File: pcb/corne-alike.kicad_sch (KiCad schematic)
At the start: 45 parts, among them SW1 SW_PUSH, SW10 SW_PUSH, SW11 SW_PUSH, SW12 SW_PUSH, SW13 SW_PUSH, SW14 SW_PUSH, SW15 SW_PUSH, SW16 SW_PUSH, SW17 SW_PUSH, SW18 SW_PUSH, SW19 SW_PUSH, SW2 SW_PUSH, SW20 SW_PUSH, SW21 SW_PUSH, SW3 SW_PUSH, SW4 SW_PUSH, SW5 SW_PUSH, SW6 SW_PUSH, SW7 SW_PUSH, SW8 SW_PUSH, SW9 SW_PUSH, U1 nice_nano

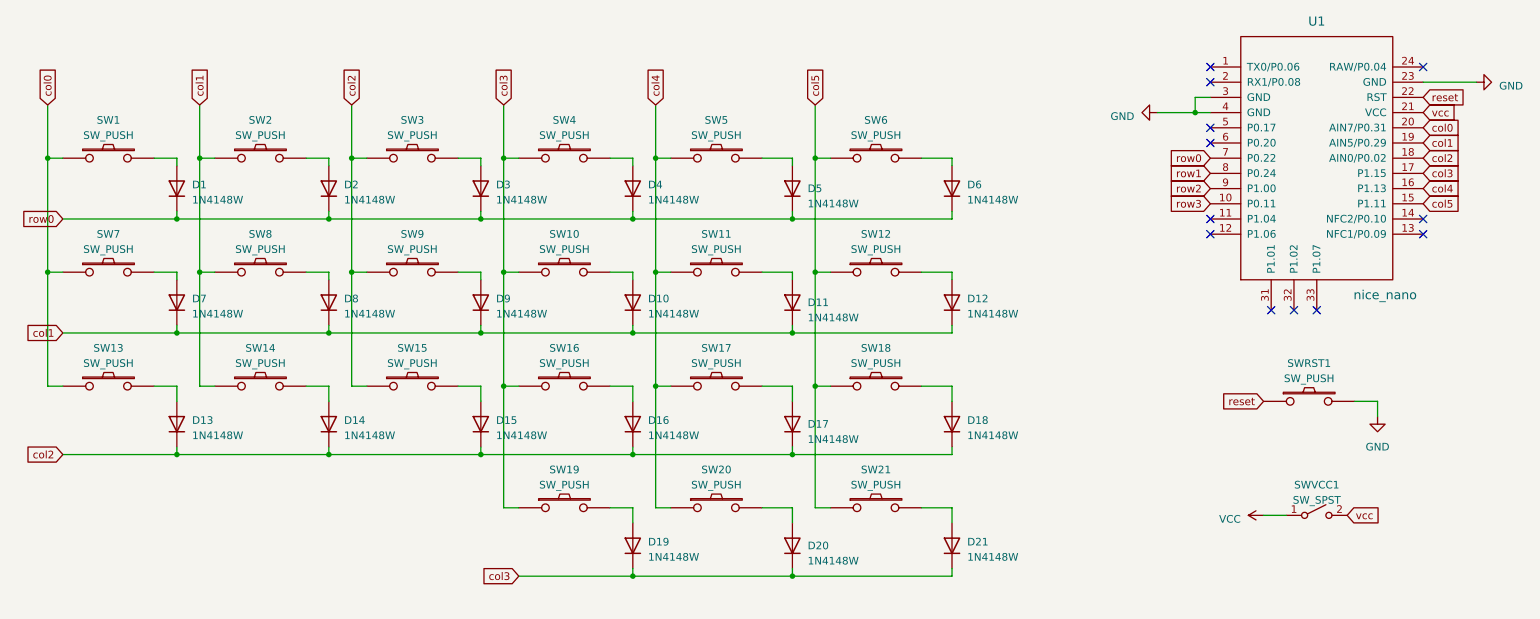
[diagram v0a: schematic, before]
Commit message: Associate footprints and generate pcb
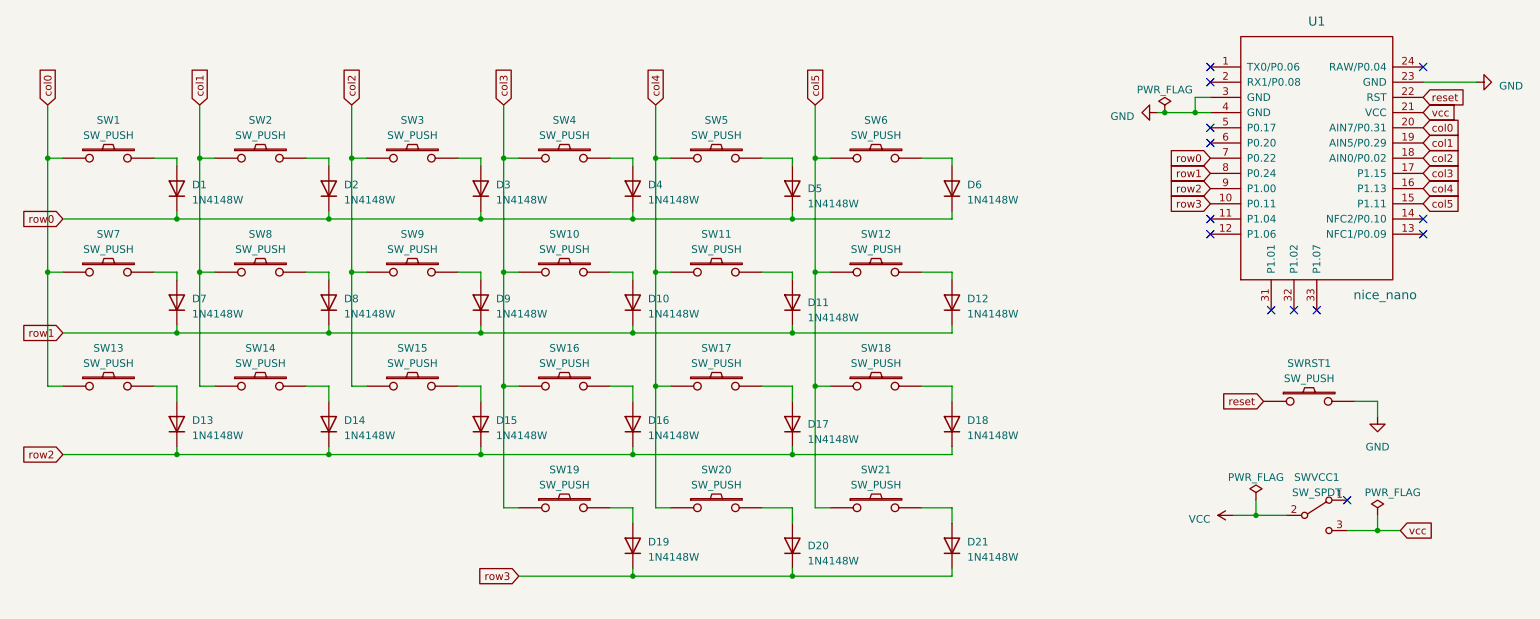
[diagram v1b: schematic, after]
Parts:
- removed SWVCC1: SW_SPST, symbol corne-alike:SW_SPST
- added SWVCC1: SW_SPDT, corne-alike:SW_EG1218, symbol corne-alike:SW_SPDT
- D1, D10, D11, D12, D13, D14, D15, D16, D17, D18, D19, D2, D20, D21, D3, D4, D5, D6, D7, D8, D9: footprint Diode_SMD:D_SOD-123 -> corne-alike:D_SOD-123
- SW1, SW10, SW11, SW12, SW13, SW14, SW15, SW16, SW17, SW18, SW19, SW2, SW20, SW21, SW3, SW4, SW5, SW6, SW7, SW8, SW9: footprint (none) -> corne-alike:Kailh_PG1350
- SWRST1: footprint (none) -> corne-alike:SW_TVBP06
- U1: footprint (none) -> corne-alike:nice_nano
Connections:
- net VCC: now also SWVCC1.2 (B)
- net col1: no longer D10.1 (K), D11.1 (K), D12.1 (K), D7.1 (K), D8.1 (K), D9.1 (K)
- net col2: no longer D13.1 (K), D14.1 (K), D15.1 (K), D16.1 (K), D17.1 (K), D18.1 (K)
- net col3: no longer D19.1 (K), D20.1 (K), D21.1 (K)
- net row1: now also D10.1 (K), D11.1 (K), D12.1 (K), D7.1 (K), D8.1 (K), D9.1 (K)
- net row2: now also D13.1 (K), D14.1 (K), D15.1 (K), D16.1 (K), D17.1 (K), D18.1 (K)
- net row3: now also D19.1 (K), D20.1 (K), D21.1 (K)
- net vcc: now also SWVCC1.3 (C)
- no-connect marks 12 -> 13

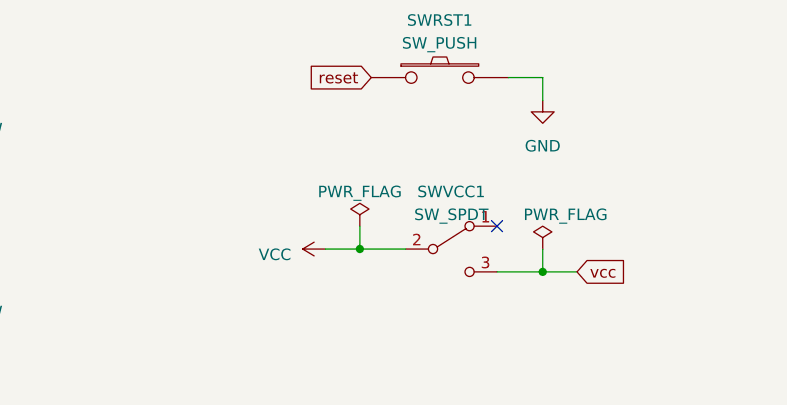
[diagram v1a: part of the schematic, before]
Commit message: Add bat connector, place reset, on/off and bat to pcb
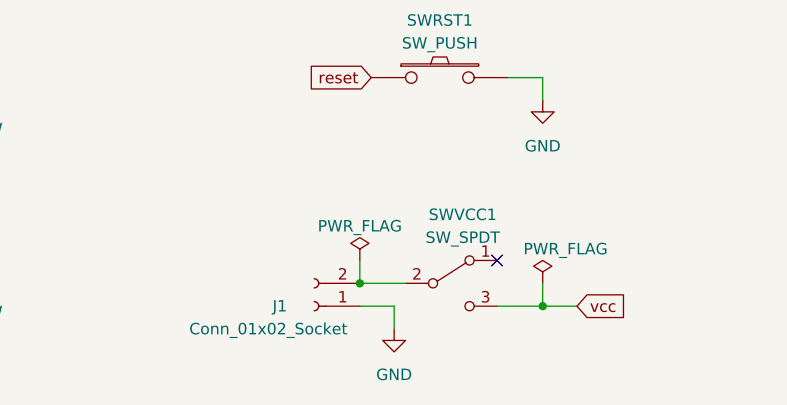
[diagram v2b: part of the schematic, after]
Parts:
- added J1: Conn_01x02_Socket, corne-alike:JST_PH_S2B-PH-SM4-TB_1x02-1MP_P2.00mm_Horizontal, symbol Connector:Conn_01x02_Socket
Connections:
- net GND: now also J1.1 (Pin_1)
- net VCC: no longer names the net of SWVCC1.2 (B)
- net VCC: now also J1.2 (Pin_2)
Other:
- moved on the sheet: SWVCC1
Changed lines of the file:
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@@
   (junction (at 120.65 107.95) (diameter 0) (color 0 0 0 0)
   )
+  (junction (at 224.79 101.6) (diameter 0) (color 0 0 0 0)
+  )
   (junction (at 95.25 48.26) (diameter 0) (color 0 0 0 0)
   )
@@
   (junction (at 99.06 57.15) (diameter 0) (color 0 0 0 0)
   )
-  (junction (at 224.79 97.79) (diameter 0) (color 0 0 0 0)
-  )
   (junction (at 95.25 67.31) (diameter 0) (color 0 0 0 0)
   )
@@
   (junction (at 151.13 38.1) (diameter 0) (color 0 0 0 0)
   )
-  (junction (at 245.11 100.33) (diameter 0) (color 0 0 0 0)
+  (junction (at 245.11 104.14) (diameter 0) (color 0 0 0 0)
   )
   (junction (at 22.86 38.1) (diameter 0) (color 0 0 0 0)
@@
   (no_connect (at 217.17 22.86))
   (no_connect (at 217.17 35.56))
-  (no_connect (at 240.03 95.25))
+  (no_connect (at 240.03 99.06))
   (no_connect (at 234.95 63.5))
   (no_connect (at 231.14 63.5))
@@
     (stroke (width 0) (type default))
   )
-  (wire (pts (xy 224.79 97.79) (xy 229.87 97.79))
+  (wire (pts (xy 224.79 101.6) (xy 229.87 101.6))
     (stroke (width 0) (type default))
   )
@@
     (stroke (width 0) (type default))
   )
+  (wire (pts (xy 228.6 106.68) (xy 228.6 104.14))
+    (stroke (width 0) (type default))
+  )
   (wire (pts (xy 25.4 87.63) (xy 44.45 87.63))
     (stroke (width 0) (type default))
@@
     (stroke (width 0) (type default))
   )
-  (wire (pts (xy 224.79 95.25) (xy 224.79 97.79))
+  (wire (pts (xy 224.79 99.06) (xy 224.79 101.6))
     (stroke (width 0) (type default))
   )
@@
     (stroke (width 0) (type default))
   )
+  (wire (pts (xy 228.6 104.14) (xy 224.79 104.14))
+    (stroke (width 0) (type default))
+  )
   (wire (pts (xy 142.24 96.52) (xy 147.32 96.52))
     (stroke (width 0) (type default))
@@
     (stroke (width 0) (type default))
   )
-  (wire (pts (xy 240.03 100.33) (xy 245.11 100.33))
+  (wire (pts (xy 240.03 104.14) (xy 245.11 104.14))
     (stroke (width 0) (type default))
   )
@@
     (stroke (width 0) (type default))
   )
-  (wire (pts (xy 245.11 97.79) (xy 245.11 100.33))
+  (wire (pts (xy 245.11 101.6) (xy 245.11 104.14))
     (stroke (width 0) (type default))
   )
@@
     (stroke (width 0) (type default))
   )
-  (wire (pts (xy 245.11 100.33) (xy 248.92 100.33))
+  (wire (pts (xy 245.11 104.14) (xy 248.92 104.14))
     (stroke (width 0) (type default))
   )
@@
     (stroke (width 0) (type default))
   )
-  (wire (pts (xy 220.98 97.79) (xy 224.79 97.79))
-    (stroke (width 0) (type default))
-  )
   (wire (pts (xy 73.66 57.15) (xy 76.2 57.15))
     (stroke (width 0) (type default))
@@
     (stroke (width 0) (type default))
   )
-  (global_label "vcc" (shape input) (at 248.92 100.33 0) (fields_autoplaced)
+  (global_label "vcc" (shape input) (at 248.92 104.14 0) (fields_autoplaced)
     (effects (font (size 1.27 1.27)) (justify left))
-    (property "Intersheetrefs" "${INTERSHEET_REFS}" (at 254.9706 100.33 0)
+    (property "Intersheetrefs" "${INTERSHEET_REFS}" (at 254.9706 104.14 0)
       (effects (font (size 1.27 1.27)) (justify left) hide)
     )
@@
     )
   )
+  (symbol (lib_id "power:GND") (at 228.6 106.68 0) (unit 1)
+    (in_bom yes) (on_board yes) (dnp no) (fields_autoplaced)
+    (property "Reference" "#PWR03" (at 228.6 113.03 0)
+      (effects (font (size 1.27 1.27)) hide)
+    )
+    (property "Value" "GND" (at 228.6 111.76 0)
+      (effects (font (size 1.27 1.27)))
+    )
+    (property "Footprint" "" (at 228.6 106.68 0)
+      (effects (font (size 1.27 1.27)) hide)
+    )
+    (property "Datasheet" "" (at 228.6 106.68 0)
+      (effects (font (size 1.27 1.27)) hide)
+    )
+    (pin "1")
+    (instances
+      (project "corne-alike"
+        (path "/0486ce6e-d8f4-41f3-afb2-9305d9ed90ac"
+          (reference "#PWR03") (unit 1)
+        )
+      )
+    )
+  )
   (symbol (lib_id "corne-alike:SW_PUSH") (at 161.29 96.52 0) (unit 1)
     (in_bom yes) (on_board yes) (dnp no) (fields_autoplaced)
@@
     )
   )
-  (symbol (lib_id "power:PWR_FLAG") (at 224.79 95.25 0) (unit 1)
+  (symbol (lib_id "power:PWR_FLAG") (at 224.79 99.06 0) (unit 1)
     (in_bom yes) (on_board yes) (dnp no)
-    (property "Reference" "#FLG01" (at 224.79 93.345 0)
-      (effects (font (size 1.27 1.27)) hide)
-    )
-    (property "Value" "PWR_FLAG" (at 224.79 91.44 0)
-      (effects (font (size 1.27 1.27)))
-    )
-    (property "Footprint" "" (at 224.79 95.25 0)
-      (effects (font (size 1.27 1.27)) hide)
-    )
-    (property "Datasheet" "~" (at 224.79 95.25 0)
+    (property "Reference" "#FLG01" (at 224.79 97.155 0)
+      (effects (font (size 1.27 1.27)) hide)
+    )
+    (property "Value" "PWR_FLAG" (at 224.79 95.25 0)
+      (effects (font (size 1.27 1.27)))
+    )
+    (property "Footprint" "" (at 224.79 99.06 0)
+      (effects (font (size 1.27 1.27)) hide)
+    )
+    (property "Datasheet" "~" (at 224.79 99.06 0)
       (effects (font (size 1.27 1.27)) hide)
     )
@@
     )
   )
-  (symbol (lib_id "corne-alike:SW_SPDT") (at 234.95 97.79 0) (unit 1)
-    (in_bom yes) (on_board yes) (dnp no) (fields_autoplaced)
-    (property "Reference" "SWVCC1" (at 234.95 91.44 0)
-      (effects (font (size 1.27 1.27)))
-    )
-    (property "Value" "SW_SPDT" (at 234.95 93.98 0)
-      (effects (font (size 1.27 1.27)))
-    )
-    (property "Footprint" "corne-alike:SW_EG1218" (at 234.95 97.79 0)
-      (effects (font (size 1.27 1.27)) hide)
-    )
-    (property "Datasheet" "~" (at 234.95 97.79 0)
+  (symbol (lib_id "corne-alike:SW_SPDT") (at 234.95 101.6 0) (unit 1)
+    (in_bom yes) (on_board yes) (dnp no)
+    (property "Reference" "SWVCC1" (at 236.22 93.98 0)
+      (effects (font (size 1.27 1.27)))
+    )
+    (property "Value" "SW_SPDT" (at 236.22 96.52 0)
+      (effects (font (size 1.27 1.27)))
+    )
+    (property "Footprint" "corne-alike:SW_EG1218" (at 234.95 101.6 0)
+      (effects (font (size 1.27 1.27)) hide)
+    )
+    (property "Datasheet" "~" (at 234.95 101.6 0)
       (effects (font (size 1.27 1.27)) hide)
     )
@@
     )
   )
+  (symbol (lib_id "Connector:Conn_01x02_Socket") (at 219.71 104.14 180) (unit 1)
+    (in_bom yes) (on_board yes) (dnp no)
+    (property "Reference" "J1" (at 215.9 104.14 0)
+      (effects (font (size 1.27 1.27)))
+    )
+    (property "Value" "Conn_01x02_Socket" (at 214.63 106.68 0)
+      (effects (font (size 1.27 1.27)))
+    )
+    (property "Footprint" "corne-alike:JST_PH_S2B-PH-SM4-TB_1x02-1MP_P2.00mm_Horizontal" (at 219.71 104.14 0)
+      (effects (font (size 1.27 1.27)) hide)
+    )
+    (property "Datasheet" "~" (at 219.71 104.14 0)
+      (effects (font (size 1.27 1.27)) hide)
+    )
+    (pin "1")
+    (pin "2")
+    (instances
+      (project "corne-alike"
+        (path "/0486ce6e-d8f4-41f3-afb2-9305d9ed90ac"
+          (reference "J1") (unit 1)
+        )
+      )
+    )
+  )
   (symbol (lib_id "corne-alike:SW_PUSH") (at 33.02 76.2 0) (unit 1)
     (in_bom yes) (on_board yes) (dnp no) (fields_autoplaced)
@@
     )
   )
-  (symbol (lib_id "power:PWR_FLAG") (at 245.11 97.79 0) (unit 1)
+  (symbol (lib_id "power:PWR_FLAG") (at 245.11 101.6 0) (unit 1)
     (in_bom yes) (on_board yes) (dnp no)
-    (property "Reference" "#FLG03" (at 245.11 95.885 0)
-      (effects (font (size 1.27 1.27)) hide)
-    )
-    (property "Value" "PWR_FLAG" (at 247.65 93.98 0)
-      (effects (font (size 1.27 1.27)))
-    )
-    (property "Footprint" "" (at 245.11 97.79 0)
-      (effects (font (size 1.27 1.27)) hide)
-    )
-    (property "Datasheet" "~" (at 245.11 97.79 0)
+    (property "Reference" "#FLG03" (at 245.11 99.695 0)
+      (effects (font (size 1.27 1.27)) hide)
+    )
+    (property "Value" "PWR_FLAG" (at 247.65 97.79 0)
+      (effects (font (size 1.27 1.27)))
+    )
+    (property "Footprint" "" (at 245.11 101.6 0)
+      (effects (font (size 1.27 1.27)) hide)
+    )
+    (property "Datasheet" "~" (at 245.11 101.6 0)
       (effects (font (size 1.27 1.27)) hide)
     )
@@
         )
       )
-    )
-  )
-  (symbol (lib_id "power:VCC") (at 220.98 97.79 90) (unit 1)
-    (in_bom yes) (on_board yes) (dnp no) (fields_autoplaced)
-    (property "Reference" "#PWR05" (at 224.79 97.79 0)
-      (effects (font (size 1.27 1.27)) hide)
-    )
-    (property "Value" "VCC" (at 217.17 98.425 90)
-      (effects (font (size 1.27 1.27)) (justify left))
-    )
-    (property "Footprint" "" (at 220.98 97.79 0)
-      (effects (font (size 1.27 1.27)) hide)
-    )
-    (property "Datasheet" "" (at 220.98 97.79 0)
-      (effects (font (size 1.27 1.27)) hide)
-    )
-    (pin "1")
-    (instances
-      (project "corne-alike"
-        (path "/0486ce6e-d8f4-41f3-afb2-9305d9ed90ac"
-          (reference "#PWR05") (unit 1)
-        )
-      )
